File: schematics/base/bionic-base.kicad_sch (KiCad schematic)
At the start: 39 parts, among them J1 Bionic_ZIF_Socket_48pin, J2 USB_C_USB2.0_16P, J3 USB_C_USB2.0_16P, J4 P1/P2, J5 P3/P4, J6 P5, J7 Debug, SW1 USR_SW, U1 TXS0108EPW, U2 TXS0108EPW, U3 TXS0108EPW, U4 TXS0108EPW, U5 TXS0108EPW, U6 SN74ACT1071DR, U7 SN74ACT1071DR

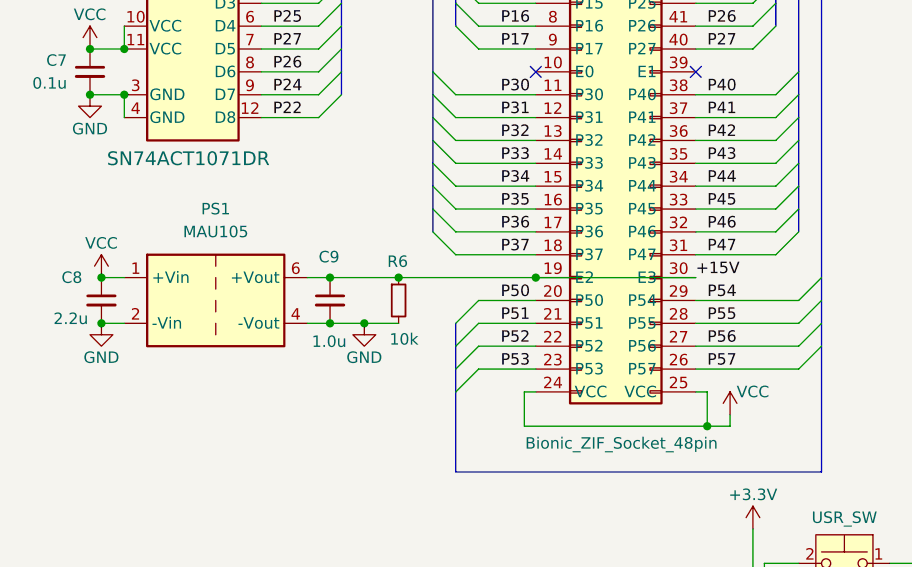
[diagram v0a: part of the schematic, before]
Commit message: [Base] Update schematics
Remove 15V DC/DC converter
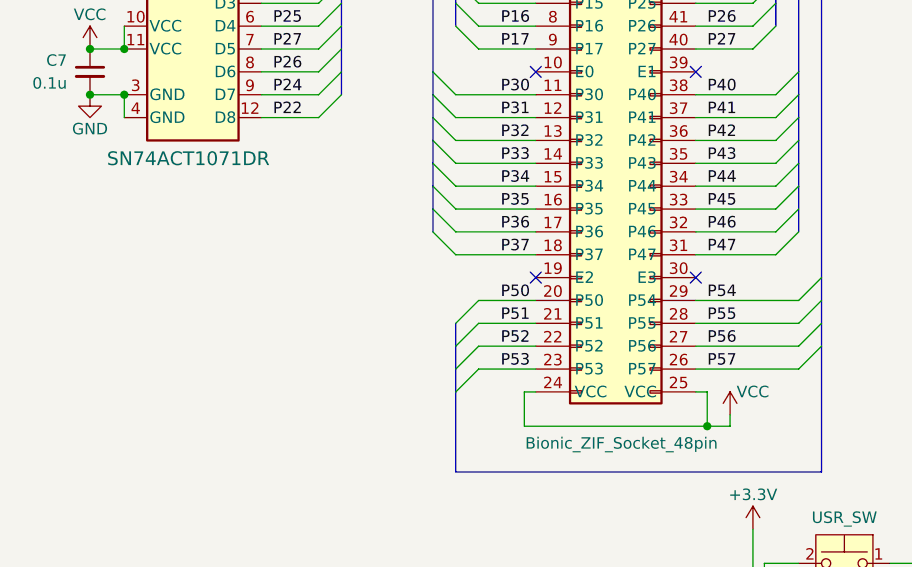
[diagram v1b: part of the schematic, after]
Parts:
- removed C8: 2.2u, Capacitor_SMD:C_0603_1608Metric_Pad1.08x0.95mm_HandSolder, symbol Device:C_Small
- removed C9: 1.0u, Capacitor_SMD:C_0603_1608Metric_Pad1.08x0.95mm_HandSolder, symbol Device:C_Small
- removed PS1: MAU105, bionic-base:Converter_DCDC_Minmax_MAU100_THT, symbol bionic-base:MAU105
- removed R6: 10k, Resistor_SMD:R_0603_1608Metric_Pad0.98x0.95mm_HandSolder, symbol Device:R_Small
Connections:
- net +15V: no longer names the net of J1.19 (E2)
- net +15V: no longer J1.30 (E3)
- no-connect marks 12 -> 14

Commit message: [Base] Cleanup Silk text
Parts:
- B1: footprint bionic-base:DIP-48_W15.24mm_Socket -> bionic-base:Teensy 4.1
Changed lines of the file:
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@@
 			)
 		)
-		(property "Footprint" "bionic-base:DIP-48_W15.24mm_Socket"
+		(property "Footprint" "bionic-base:Teensy 4.1"
 			(at 175.26 137.16 0)
 			(effects
